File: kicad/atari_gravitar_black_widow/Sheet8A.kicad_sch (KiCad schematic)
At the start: 88 parts, among them Q11 2N3906, Q12 2N3904

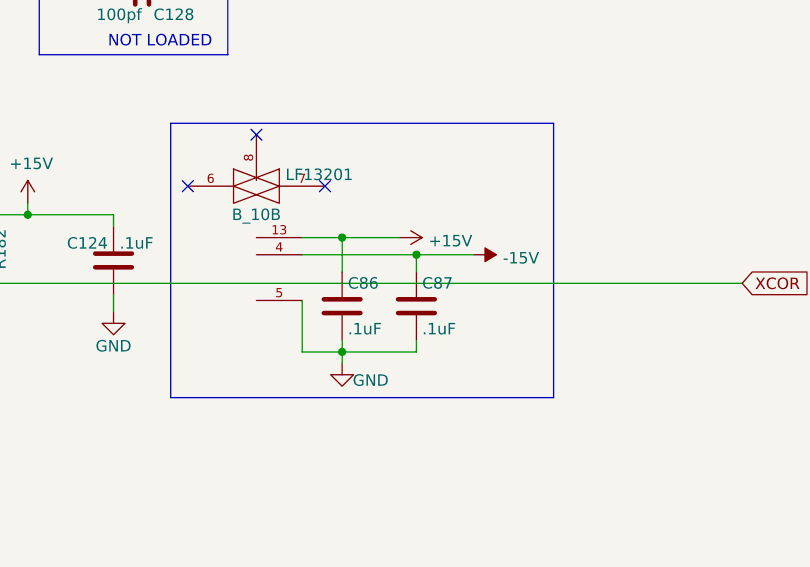
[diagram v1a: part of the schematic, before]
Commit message: Fixed ERC errors and added traces to the edge connectors
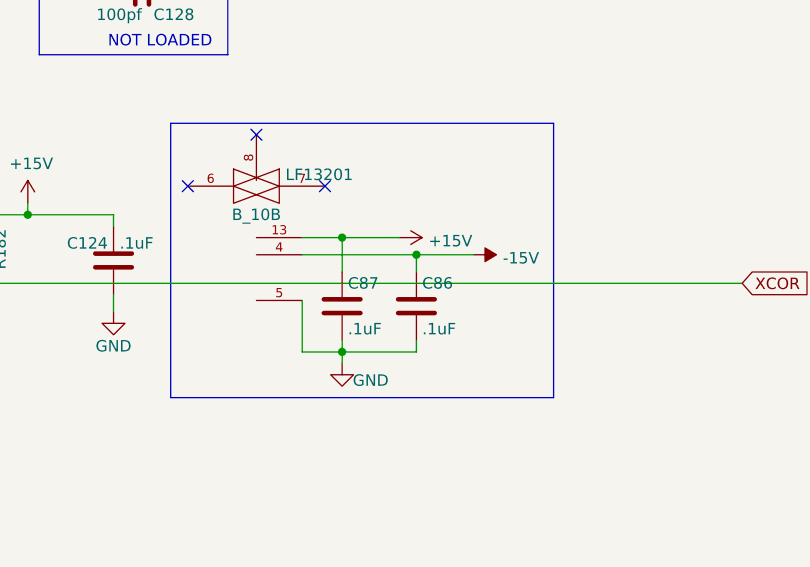
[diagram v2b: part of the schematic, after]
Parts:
- renumbered C87 to C86, C86 to C87
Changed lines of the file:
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@@
   (symbol (lib_id "Device:C") (at 527.685 153.67 0) (unit 1)
     (in_bom yes) (on_board yes)
-    (property "Reference" "C87" (id 0) (at 528.32 151.13 0)
+    (property "Reference" "C86" (id 0) (at 528.32 151.13 0)
       (effects (font (size 1.27 1.27)) (justify left))
     )
@@
   (symbol (lib_id "Device:C") (at 519.43 153.67 0) (unit 1)
     (in_bom yes) (on_board yes)
-    (property "Reference" "C86" (id 0) (at 520.065 151.13 0)
-      (effects (font (size 1.27 1.27)) (justify left))
-    )
+    (property "Reference" "C87" (id 0) (at 520.065 151.13 0)
+      (effects (font (size 1.27 1.27)) (justify left))
+    )

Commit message: Analog
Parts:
- renumbered D/E_1 to D/E_11
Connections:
- net XBIP: now also R99.3; no longer R99.1
- net YBIP: now also R98.3; no longer R98.1
- net at R165.1: now also R98.1; no longer R98.3
- net at R168.1: now also R99.1; no longer R99.3
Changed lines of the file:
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@@
     (pin "1")
   )
-  (symbol (lib_id "atari_grav_bw:POT") (at 222.25 193.04 270) (unit 1)
-    (in_bom yes) (on_board yes)
-    (property "Reference" "R98" (id 0) (at 224.663 191.008 90)
+  (symbol (lib_name "POT_2") (lib_id "atari_grav_bw:POT") (at 222.25 193.04 270) (unit 1)
+    (in_bom yes) (on_board yes)
+    (property "Reference" "R98" (id 0) (at 224.1744 191.109 90)
       (effects (font (size 1.27 1.27)) (justify right))
     )
-    (property "Value" "500" (id 1) (at 223.901 193.04 90)
+    (property "Value" "500" (id 1) (at 224.1549 193.0403 90)
       (effects (font (size 1.27 1.27)) (justify right))
     )
@@
   (symbol (lib_id "atari_grav_bw:082") (at 546.735 84.455 0) (mirror x) (unit 1)
     (in_bom yes) (on_board yes)
-    (property "Reference" "D/E_1" (id 0) (at 542.036 83.947 0)
+    (property "Reference" "D/E_11" (id 0) (at 542.036 83.947 0)
       (effects (font (size 1.27 1.27)) (justify left))
     )
@@
   (symbol (lib_id "atari_grav_bw:082") (at 498.475 81.915 0) (unit 2)
     (in_bom yes) (on_board yes)
-    (property "Reference" "D/E_1" (id 0) (at 497.459 81.407 0))
+    (property "Reference" "D/E_11" (id 0) (at 497.459 81.407 0))
     (property "Value" "082" (id 1) (at 496.57 83.312 0))
     (property "Footprint" "Star_Wars_Vector_PCB:DIP8" (id 2) (at 498.475 81.915 0)
@@
     (pin "1")
   )
-  (symbol (lib_id "atari_grav_bw:POT") (at 222.25 214.63 270) (unit 1)
-    (in_bom yes) (on_board yes)
-    (property "Reference" "R99" (id 0) (at 224.663 212.598 90)
+  (symbol (lib_name "POT_1") (lib_id "atari_grav_bw:POT") (at 222.25 214.63 270) (unit 1)
+    (in_bom yes) (on_board yes)
+    (property "Reference" "R99" (id 0) (at 224.1951 212.6373 90)
       (effects (font (size 1.27 1.27)) (justify right))
     )
-    (property "Value" "500" (id 1) (at 223.901 214.63 90)
+    (property "Value" "500" (id 1) (at 224.0942 214.6542 90)
       (effects (font (size 1.27 1.27)) (justify right))
     )

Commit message: finished most all traces in analog
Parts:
- R187, R189, R192: footprint Star_Wars_Vector_PCB:PotBlue -> Star_Wars_Vector_PCB:PotBlk
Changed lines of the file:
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@@
       (effects (font (size 1.27 1.27)) (justify right))
     )
-    (property "Footprint" "Star_Wars_Vector_PCB:PotBlue" (id 2) (at 475.615 104.775 0)
+    (property "Footprint" "Star_Wars_Vector_PCB:PotBlk" (id 2) (at 475.615 104.775 0)
       (effects (font (size 1.27 1.27)) hide)
     )
@@
       (effects (font (size 1.27 1.27)) (justify right))
     )
-    (property "Footprint" "Star_Wars_Vector_PCB:PotBlue" (id 2) (at 523.875 81.915 0)
+    (property "Footprint" "Star_Wars_Vector_PCB:PotBlk" (id 2) (at 523.875 81.915 0)
       (effects (font (size 1.27 1.27)) hide)
     )
@@
       (effects (font (size 1.27 1.27)) (justify right))
     )
-    (property "Footprint" "Star_Wars_Vector_PCB:PotBlue" (id 2) (at 451.485 104.775 0)
-      (effects (font (size 1.27 1.27)) hide)
-    )
+    (property "Footprint" "Star_Wars_Vector_PCB:PotBlk" (id 2) (at 451.485 104.775 0)
+      (effects (font (size 1.27 1.27)) hide)
+    )

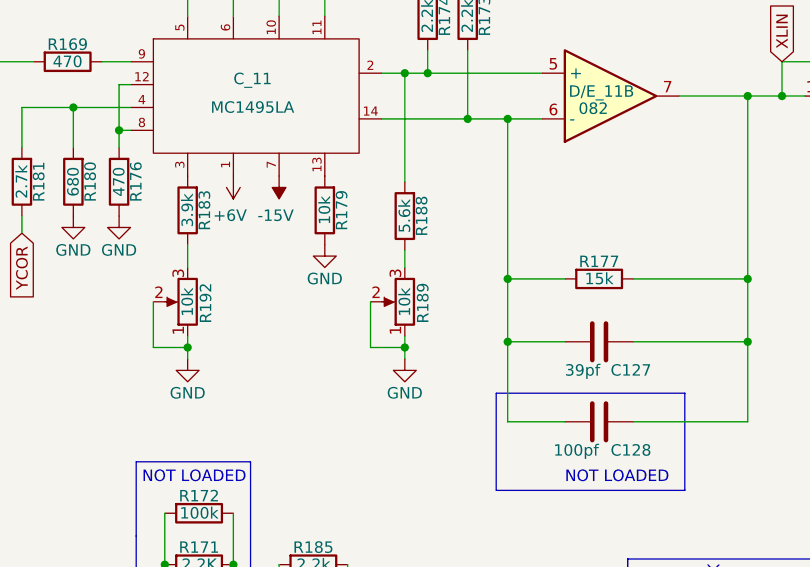
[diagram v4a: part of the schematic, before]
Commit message: Analog done but for rev 2 R/Cs
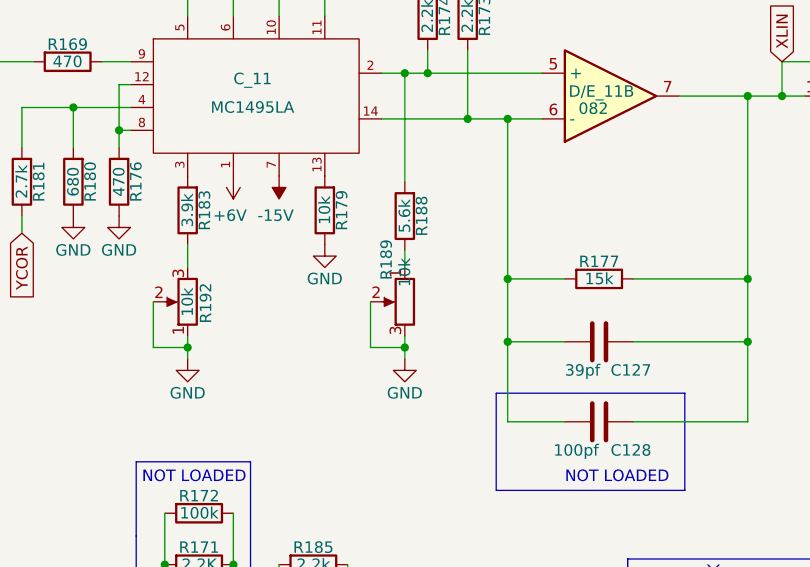
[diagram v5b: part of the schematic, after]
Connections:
- net GND: now also R189.3; no longer R189.1
- net at R188.1: now also R189.1; no longer R189.3
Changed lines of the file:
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@@
     (pin "1")
   )
-  (symbol (lib_id "atari_grav_bw:POT") (at 475.615 104.775 180) (unit 1)
-    (in_bom yes) (on_board yes)
-    (property "Reference" "R189" (id 0) (at 477.647 107.188 90)
+  (symbol (lib_name "POT_4") (lib_id "atari_grav_bw:POT") (at 475.615 104.775 180) (unit 1)
+    (in_bom yes) (on_board yes)
+    (property "Reference" "R189" (id 0) (at 473.583 102.362 90)
       (effects (font (size 1.27 1.27)) (justify right))
     )
-    (property "Value" "10k" (id 1) (at 475.615 106.426 90)
+    (property "Value" "10k" (id 1) (at 475.615 103.124 90)
       (effects (font (size 1.27 1.27)) (justify right))
     )
@@
     (pin "2")
   )
-  (symbol (lib_id "atari_grav_bw:POT") (at 451.485 104.775 180) (unit 1)
+  (symbol (lib_name "POT_3") (lib_id "atari_grav_bw:POT") (at 451.485 104.775 180) (unit 1)
     (in_bom yes) (on_board yes)
     (property "Reference" "R192" (id 0) (at 453.517 107.188 90)
@@
       (effects (font (size 1.27 1.27)) hide)
     )
-    (pin "1")
-    (pin "2")
     (pin "3")
+    (pin "2")
+    (pin "1")
   )
   (symbol (lib_id "power:-15V") (at 150.495 245.11 270) (unit 1)

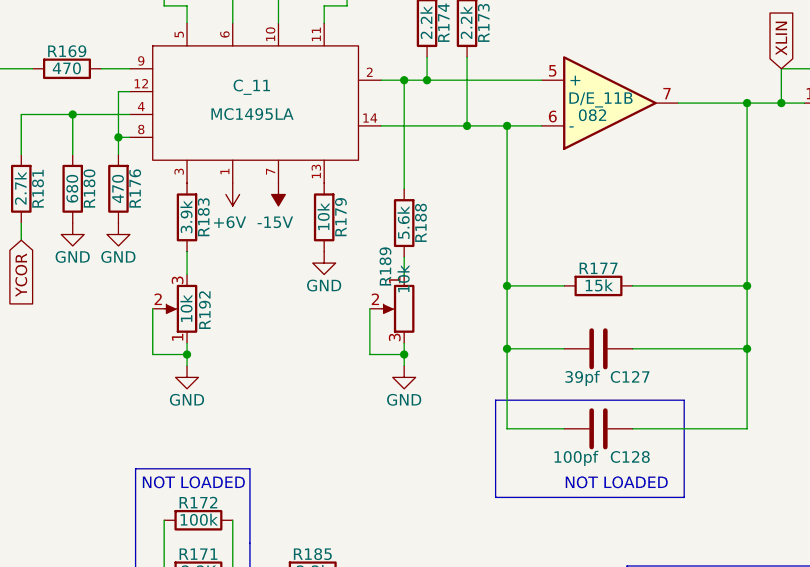
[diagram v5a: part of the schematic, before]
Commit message: Just need grounds and rev 2 resistors
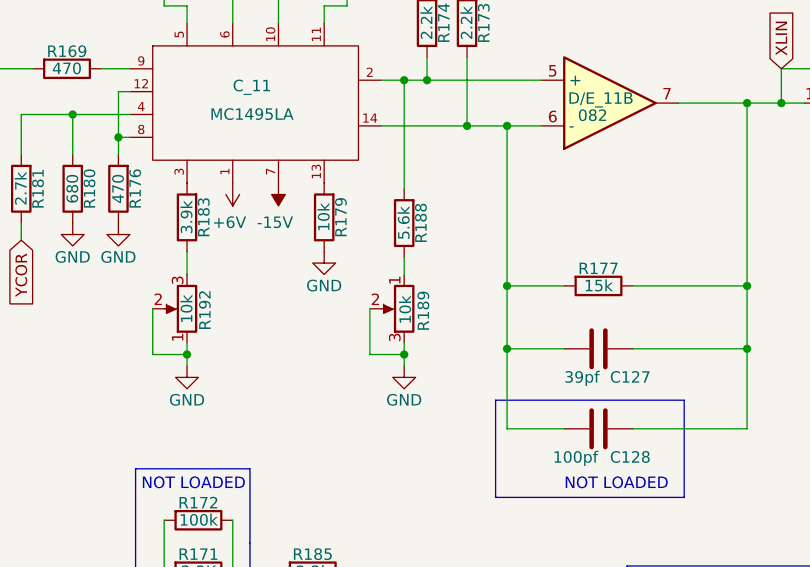
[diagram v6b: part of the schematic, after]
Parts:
- C128: footprint Star_Wars_Vector_PCB:GenericComp -> Star_Wars_Vector_PCB:CapBrown
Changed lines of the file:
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@@
   (symbol (lib_name "POT_4") (lib_id "atari_grav_bw:POT") (at 475.615 104.775 180) (unit 1)
     (in_bom yes) (on_board yes)
-    (property "Reference" "R189" (id 0) (at 473.583 102.362 90)
+    (property "Reference" "R189" (id 0) (at 477.7898 107.2797 90)
       (effects (font (size 1.27 1.27)) (justify right))
     )
-    (property "Value" "10k" (id 1) (at 475.615 103.124 90)
+    (property "Value" "10k" (id 1) (at 475.7739 106.5044 90)
       (effects (font (size 1.27 1.27)) (justify right))
     )
@@
       (effects (font (size 1.27 1.27)) hide)
     )
+    (pin "1")
+    (pin "2")
     (pin "3")
-    (pin "2")
-    (pin "1")
   )
   (symbol (lib_id "power:-15V") (at 150.495 245.11 270) (unit 1)
@@
       (effects (font (size 1.27 1.27)) (justify left))
     )
-    (property "Footprint" "Star_Wars_Vector_PCB:GenericComp" (id 2) (at 493.395 119.0752 0)
-      (effects (font (size 1.27 1.27)) hide)
-    )
+    (property "Footprint" "Star_Wars_Vector_PCB:CapBrown" (id 2) (at 493.395 119.0752 0)
+      (effects (font (size 1.27 1.27)) hide)
+    )

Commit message: second to last cleanup?
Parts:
- added C137: 1000pf, Star_Wars_Vector_PCB:CapBrown, symbol Device:C
- R162, R163: value 7K -> 7.5K
- R172: value 100k -> ?
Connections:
- net GND: now also C137.1
- net XBIP: now also C137.2
- net XLIN: no longer names the net of C127.1, C128.1, D/E_11.7, R177.1, R187.1, R187.2
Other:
- note added: "X Center"
- note added: "X Linearity"
- note added: "X Size"
- moved on the sheet: B_10B, C86, C87

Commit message: Fixed various issues and generated gerber files
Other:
- moved on the sheet: R189, R98, R99
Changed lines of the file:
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@@
     (pin "1")
   )
-  (symbol (lib_name "POT_4") (lib_id "atari_grav_bw:POT") (at 475.615 104.775 180) (unit 1)
-    (in_bom yes) (on_board yes)
-    (property "Reference" "R189" (id 0) (at 477.7898 107.2797 90)
+  (symbol (lib_id "atari_grav_bw:POT") (at 475.615 104.775 0) (mirror y) (unit 1)
+    (in_bom yes) (on_board yes)
+    (property "Reference" "R189" (id 0) (at 477.7898 102.2703 90)
       (effects (font (size 1.27 1.27)) (justify right))
     )
-    (property "Value" "10k" (id 1) (at 475.7739 106.5044 90)
+    (property "Value" "10k" (id 1) (at 475.7739 103.0456 90)
       (effects (font (size 1.27 1.27)) (justify right))
     )
@@
     (pin "1")
   )
-  (symbol (lib_name "POT_2") (lib_id "atari_grav_bw:POT") (at 222.25 193.04 270) (unit 1)
-    (in_bom yes) (on_board yes)
-    (property "Reference" "R98" (id 0) (at 224.1744 191.109 90)
+  (symbol (lib_id "atari_grav_bw:POT") (at 222.25 193.04 90) (mirror x) (unit 1)
+    (in_bom yes) (on_board yes)
+    (property "Reference" "R98" (id 0) (at 220.3256 191.109 90)
       (effects (font (size 1.27 1.27)) (justify right))
     )
-    (property "Value" "500" (id 1) (at 224.1549 193.0403 90)
+    (property "Value" "500" (id 1) (at 220.3451 193.0403 90)
       (effects (font (size 1.27 1.27)) (justify right))
     )
@@
     (pin "1")
   )
-  (symbol (lib_name "POT_1") (lib_id "atari_grav_bw:POT") (at 222.25 214.63 270) (unit 1)
-    (in_bom yes) (on_board yes)
-    (property "Reference" "R99" (id 0) (at 224.1951 212.6373 90)
+  (symbol (lib_id "atari_grav_bw:POT") (at 222.25 214.63 90) (mirror x) (unit 1)
+    (in_bom yes) (on_board yes)
+    (property "Reference" "R99" (id 0) (at 220.3049 212.6373 90)
       (effects (font (size 1.27 1.27)) (justify right))
     )
-    (property "Value" "500" (id 1) (at 224.0942 214.6542 90)
+    (property "Value" "500" (id 1) (at 220.4058 214.6542 90)
       (effects (font (size 1.27 1.27)) (justify right))
     )
@@
     (pin "2")
   )
-  (symbol (lib_name "POT_3") (lib_id "atari_grav_bw:POT") (at 451.485 104.775 180) (unit 1)
+  (symbol (lib_id "atari_grav_bw:POT") (at 451.485 104.775 180) (unit 1)
     (in_bom yes) (on_board yes)
     (property "Reference" "R192" (id 0) (at 453.517 107.188 90)
